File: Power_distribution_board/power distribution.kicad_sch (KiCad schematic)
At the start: 17 parts, among them J1 Pin headers, J10 XT30 Connector, J2 Pin headers, J3 Pin headers, J4 Pin headers, J6 Pin headers, J7 Pin headers, J8 Pin headers, J9 XT30 Connector, SW2 SW_SPST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

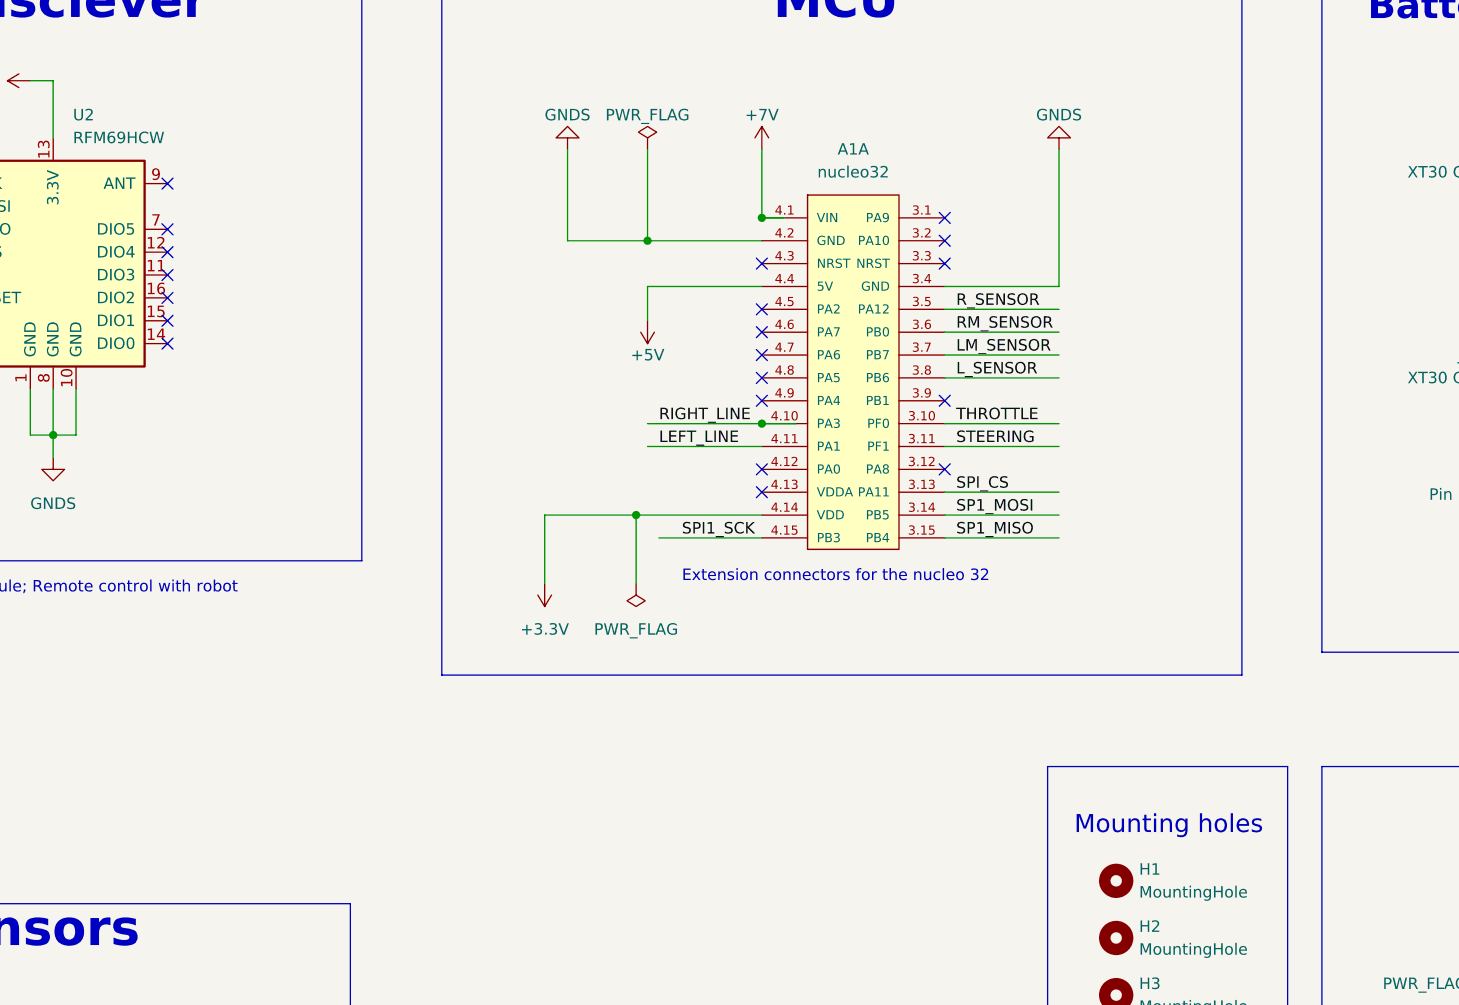
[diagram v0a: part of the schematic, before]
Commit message: added new switch footprint, update gerbers
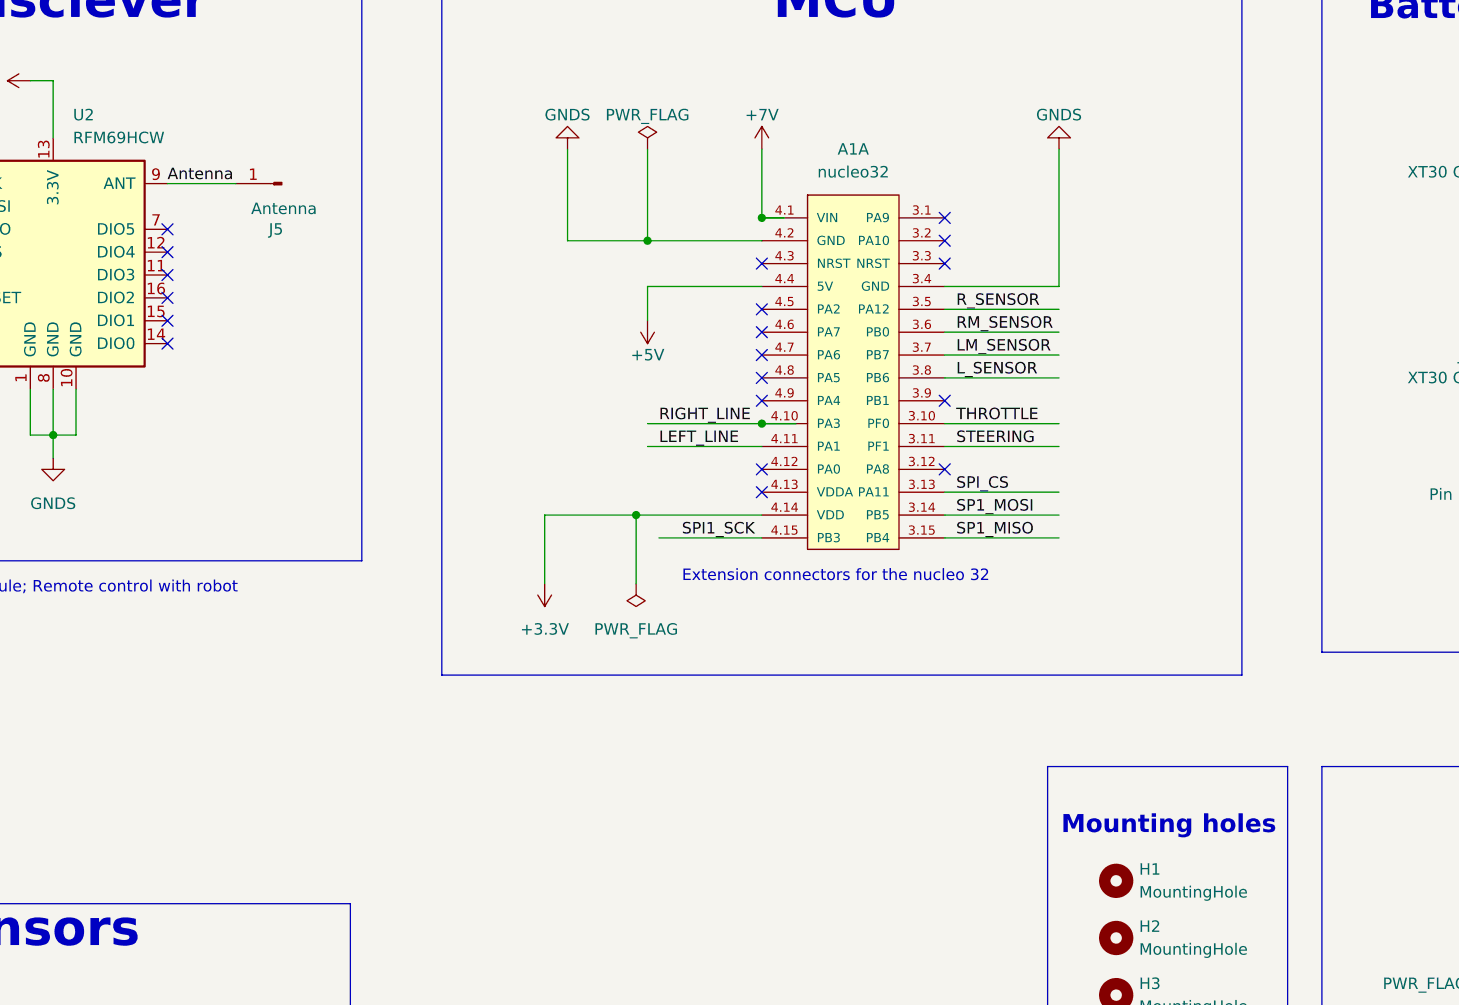
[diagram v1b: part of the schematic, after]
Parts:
- added J5: Antenna, Connector_Wire:SolderWire-0.1sqmm_1x01_D0.4mm_OD1mm, symbol Connector:Conn_01x01_Pin
- SW2: footprint Button_Switch_THT:SW_E-Switch_EG1271_SPDT -> GH36P010001:GH36P010001_APM
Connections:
- net Antenna: now reaches U2.9 (ANT)
- net Antenna: now also J5.1 (Pin_1)
- no-connect marks 26 -> 25
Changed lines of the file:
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@@
 	(title_block
 		(title "Sumo Robot Controller ")
-		(date "2024-06-06")
+		(date "2024-07-04")
 		(rev "2")
 	)
@@
 	)
 	(no_connect
-		(at 76.2 45.72)
-	)
-	(no_connect
 		(at 226.06 88.9)
 	)
@@
 	(wire
 		(pts
+			(xy 76.2 45.72) (xy 83.82 45.72)
+		)
+		(stroke
+			(width 0)
+			(type default)
+		)
+	)
+	(wire
+		(pts
 			(xy 242.57 57.15) (xy 245.11 57.15)
 		)
@@
 			(font
 				(size 2 2)
+				(thickness 0.4)
+				(bold yes)
 			)
 		)
@@
 		)
 	)
+	(label "Antenna"
+		(at 76.2 45.72 0)
+		(fields_autoplaced yes)
+		(effects
+			(font
+				(size 1.27 1.27)
+			)
+			(justify left bottom)
+		)
+	)
 	(label "SP1_MISO"
 		(at 40.64 50.8 0)
@@
 	)
 	(symbol
+		(lib_id "Connector:Conn_01x01_Pin")
+		(at 88.9 45.72 180)
+		(unit 1)
+		(exclude_from_sim no)
+		(in_bom yes)
+		(on_board yes)
+		(dnp no)
+		(property "Reference" "J5"
+			(at 88.265 50.8 0)
+			(effects
+				(font
+					(size 1.27 1.27)
+				)
+			)
+		)
+		(property "Value" "Antenna"
+			(at 89.154 48.514 0)
+			(effects
+				(font
+					(size 1.27 1.27)
+				)
+			)
+		)
+		(property "Footprint" "Connector_Wire:SolderWire-0.1sqmm_1x01_D0.4mm_OD1mm"
+			(at 88.9 45.72 0)
+			(effects
+				(font
+					(size 1.27 1.27)
+				)
+				(hide yes)
+			)
+		)
+		(property "Datasheet" "~"
+			(at 88.9 45.72 0)
+			(effects
+				(font
+					(size 1.27 1.27)
+				)
+				(hide yes)
+			)
+		)
+		(property "Description" "Generic connector, single row, 01x01, script generated"
+			(at 88.9 45.72 0)
+			(effects
+				(font
+					(size 1.27 1.27)
+				)
+				(hide yes)
+			)
+		)
+		(pin "1"
+		)
+		(instances
+			(project "power distribution"
+				(path "/1ade6856-1148-42e0-ba7f-851ea6fd76dc"
+					(reference "J5")
+					(unit 1)
+				)
+			)
+		)
+	)
+	(symbol
 		(lib_id "0_sumo_power:GNDS")
 		(at 49.53 146.05 0)
@@
 			)
 		)
-		(property "Footprint" "Button_Switch_THT:SW_E-Switch_EG1271_SPDT"
+		(property "Footprint" "GH36P010001:GH36P010001_APM"
 			(at 237.49 57.15 0)
 			(effects

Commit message: update backups
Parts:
- J10, J9: symbol Connector:Conn_01x02_Socket -> Connector_Generic:Conn_01x02
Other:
- moved on the sheet: J10, J9
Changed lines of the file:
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@@
 	)
 	(symbol
-		(lib_id "Connector:Conn_01x02_Socket")
+		(lib_id "Connector_Generic:Conn_01x02")
 		(at 220.98 50.8 180)
 		(unit 1)
@@
 			)
 		)
-		(property "Description" ""
+		(property "Description" "Generic connector, single row, 01x02, script generated (kicad-library-utils/schlib/autogen/connector/)"
 			(at 220.98 50.8 0)
 			(effects
@@
 	)
 	(symbol
-		(lib_id "Connector:Conn_01x02_Socket")
+		(lib_id "Connector_Generic:Conn_01x02")
 		(at 220.98 72.39 180)
 		(unit 1)
@@
 			)
 		)
-		(property "Description" ""
+		(property "Description" "Generic connector, single row, 01x02, script generated (kicad-library-utils/schlib/autogen/connector/)"
 			(at 220.98 72.39 0)
 			(effects
